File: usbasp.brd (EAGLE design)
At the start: 34.8 x 23.3 mm, 21 parts, among them J1 JISP, Y1 12MHz

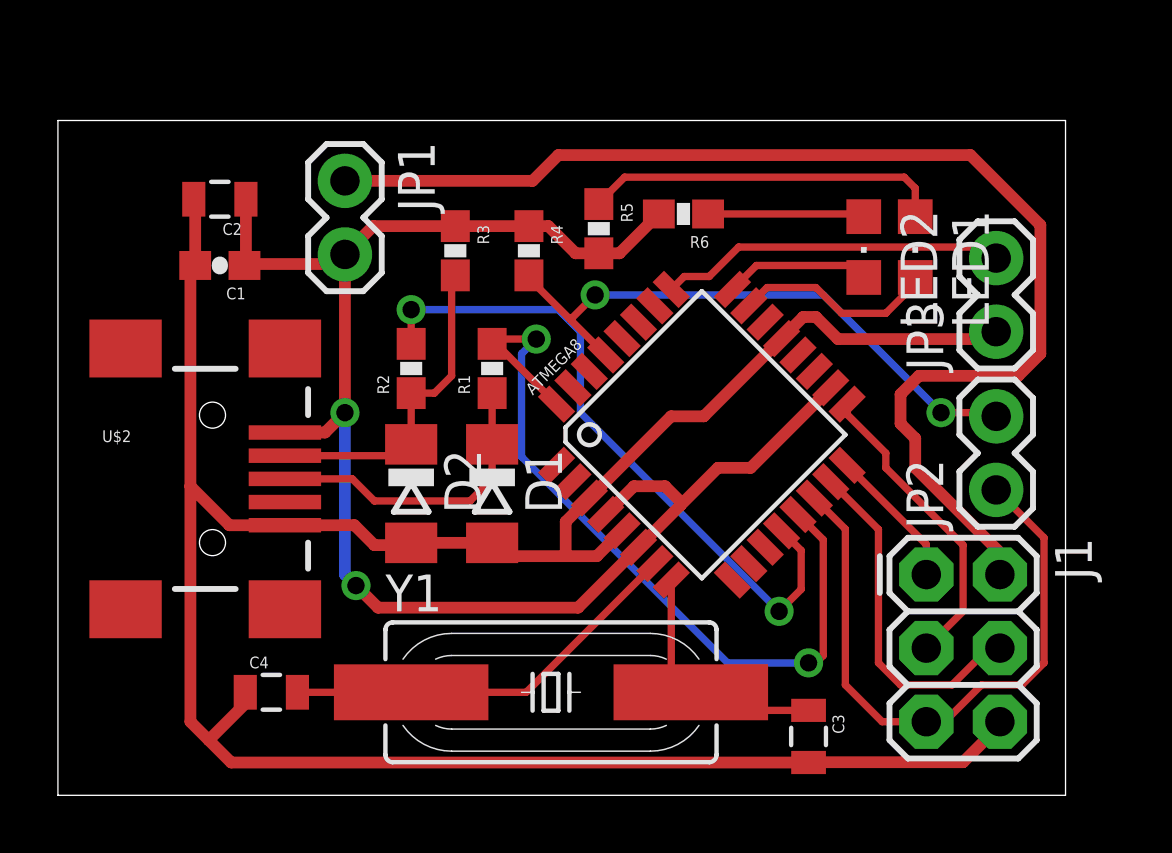
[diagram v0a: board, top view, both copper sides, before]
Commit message: Make the board a bit smaller
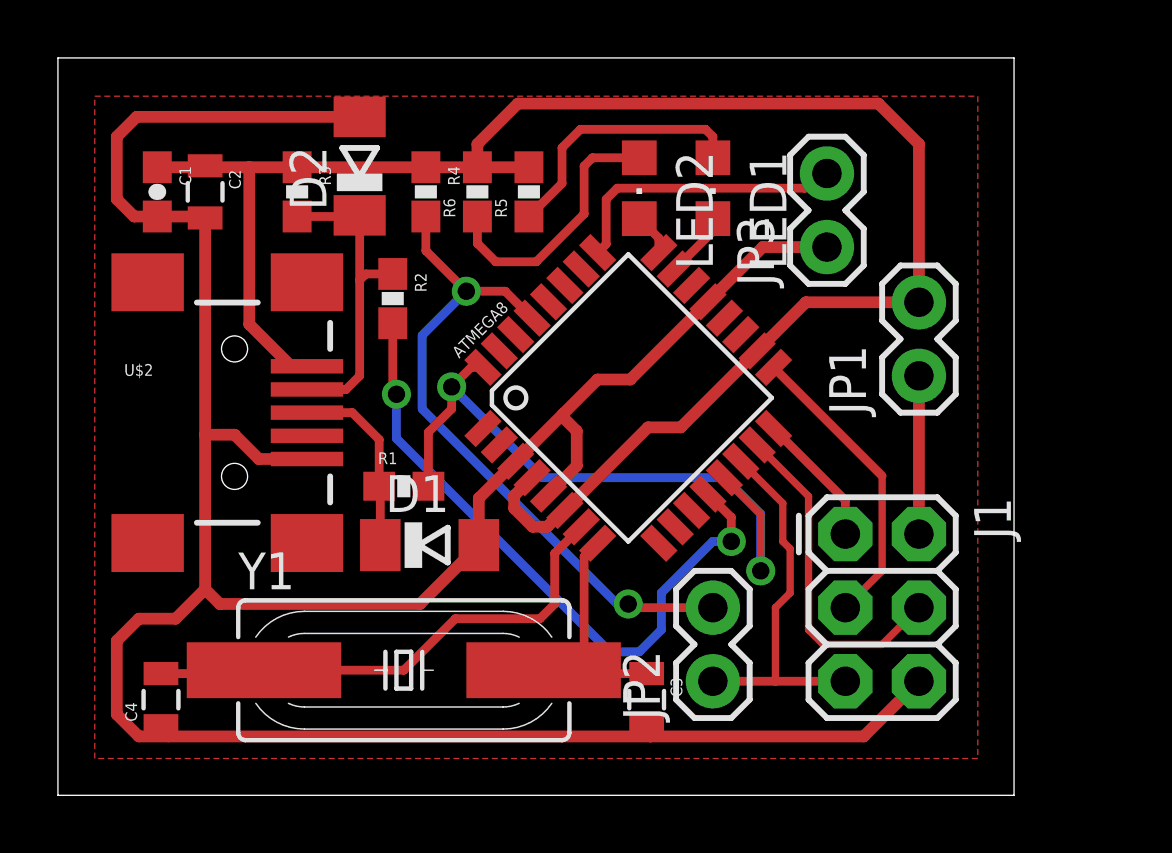
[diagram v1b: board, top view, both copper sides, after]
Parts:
- moved JP1 20.9 mm to (29.7, 14.5), turned to 90 degrees
- moved JP2 11.8 mm to (22.6, 3.94)
- moved D2 11.4 mm to (10.4, 21.7), turned to 90 degrees
- moved LED2 8.01 mm to (20.1, 21.0)
- moved LED1 7.27 mm to (22.6, 21.0)
- moved R6 7.15 mm to (14.5, 20.8), turned to 90 degrees
- moved JP3 6.53 mm to (26.5, 18.9)
- moved R3 5.83 mm to (8.26, 20.8)
- moved C3 5.73 mm to (20.3, 3.30)
- moved Y1 5.14 mm to (11.9, 4.32)
- moved R1 5.08 mm to (11.9, 10.7), turned to 0 degrees
- moved R4 4.10 mm to (12.7, 20.8)
- moved C4 3.82 mm to (3.56, 3.30), turned to 90 degrees
- moved C1 3.33 mm to (3.43, 20.8), turned to 270 degrees
- moved J1 3.12 mm to (27.2, 9.02)
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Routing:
- net VCCIN: track 42.9 -> 5.46 mm
- net GND: track 85.6 -> 97.9 mm
- net N$5: track 21.8 -> 13.1 mm
- net VCC: track 55.2 -> 62.3 mm, vias 2 -> 0
- net N$6: track 7.02 -> 2.28 mm
- net D+: track 27.6 -> 23.3 mm
- net N$2: track 10.7 -> 6.54 mm
- net N$9: track 5.41 -> 9.23 mm
- net N$7: track 5.07 -> 1.45 mm
- net N$3: track 14.2 -> 17.6 mm
- net N$8: track 12.5 -> 9.15 mm
- net RST: track 20.6 -> 23.4 mm
- net N$10: track 12.0 -> 9.95 mm
- added copper zone on layer 1, net GND
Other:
- board size 34.8 x 23.3 mm -> 33 x 25.5 mm
